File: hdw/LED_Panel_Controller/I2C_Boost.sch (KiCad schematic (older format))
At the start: 7 parts, among them U1301 LTC1694, U1302 AT24CS32-STUM, U1303 MCP9804

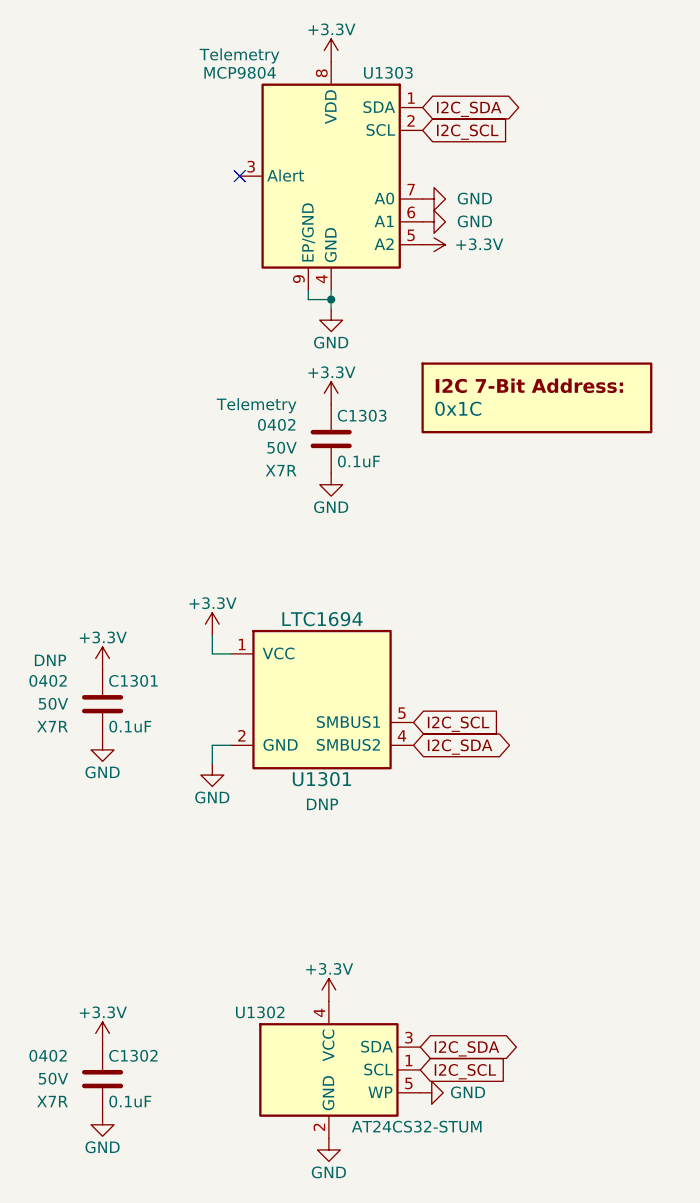
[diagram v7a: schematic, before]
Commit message: separated function groups on PCB
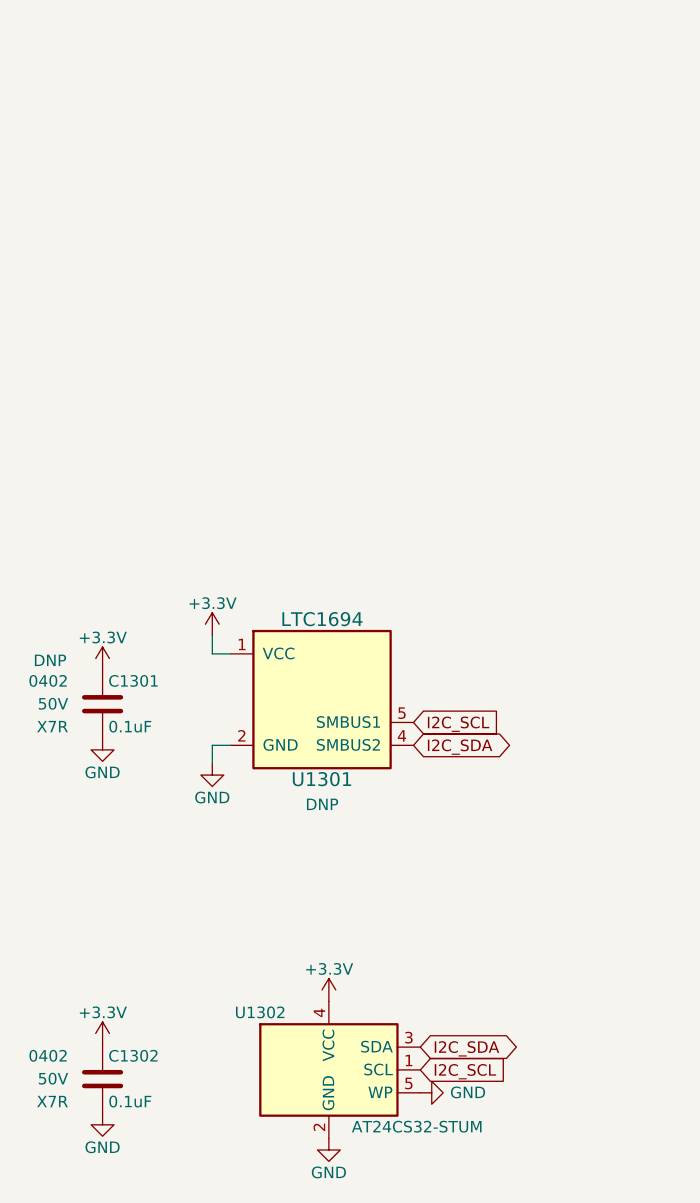
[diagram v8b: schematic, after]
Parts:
- removed C1303: 0.1uF, Capacitors_SMD:C_0402, symbol Custom_Library:C_Custom
- removed DOC1301: 0x1C, symbol Custom_Library:I2C_Address
- removed U1303: MCP9804, Package_DFN_QFN:DFN-8-1EP_3x2mm_P0.5mm_EP1.3x1.5mm, symbol Sensor_Temperature:MCP9804_DFN
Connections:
- no-connect marks 1 -> 0
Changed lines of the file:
@@
 	0    -1   -1   0
 $EndComp
-$Comp
-L power:GND #PWR?
-U 1 1 6061CC13
-P 5340 2050
-AR Path="/5B3E071A/6061CC13" Ref="#PWR?"  Part="1"
-AR Path="/5E0652BA/6061CC13" Ref="#PWR?"  Part="1"
-AR Path="/5E0A0E29/6061CC13" Ref="#PWR?"  Part="1"
-AR Path="/5E052856/6061CC13" Ref="#PWR?"  Part="1"
-AR Path="/5EAE2D84/6061CC13" Ref="#PWR?"  Part="1"
-AR Path="/5F581B58/6061CC13" Ref="#PWR?"  Part="1"
-AR Path="/5F581B77/6061CC13" Ref="#PWR?"  Part="1"
-AR Path="/5F581BB7/6061CC13" Ref="#PWR?"  Part="1"
-AR Path="/5F582A7C/6061CC13" Ref="#PWR01310"  Part="1"
-F 0 "#PWR01310" H 5340 1800 50  0001 C CNN
-F 1 "GND" H 5340 1900 50  0000 C CNN
-F 2 "" H 5340 2050 50  0001 C CNN
-F 3 "" H 5340 2050 50  0001 C CNN
-	1    5340 2050
-	-1   0    0    -1
-$EndComp
-Wire Wire Line
-	5340 2050 5340 2010
-Wire Wire Line
-	5340 2010 5340 1970
-Wire Wire Line
-	5340 2010 5240 2010
-Wire Wire Line
-	5240 2010 5240 1970
-Connection ~ 5340 2010
-$Comp
-L power:+3.3V #PWR?
-U 1 1 6061CC1E
-P 5340 970
-AR Path="/5E0652BA/6061CC1E" Ref="#PWR?"  Part="1"
-AR Path="/5E0A0E29/6061CC1E" Ref="#PWR?"  Part="1"
-AR Path="/5E052856/6061CC1E" Ref="#PWR?"  Part="1"
-AR Path="/5EAE2D84/6061CC1E" Ref="#PWR?"  Part="1"
-AR Path="/5F581B58/6061CC1E" Ref="#PWR?"  Part="1"
-AR Path="/5F581B77/6061CC1E" Ref="#PWR?"  Part="1"
-AR Path="/5F581BB7/6061CC1E" Ref="#PWR?"  Part="1"
-AR Path="/5F582A7C/6061CC1E" Ref="#PWR01309"  Part="1"
-F 0 "#PWR01309" H 5340 820 50  0001 C CNN
-F 1 "+3.3V" H 5340 1110 50  0000 C CNN
-F 2 "" H 5340 970 50  0001 C CNN
-F 3 "" H 5340 970 50  0001 C CNN
-	1    5340 970
-	-1   0    0    -1
-$EndComp
-$Comp
-L Sensor_Temperature:MCP9804_DFN U?
-U 1 1 6061CC26
-P 5340 1470
-AR Path="/5B3E071A/6061CC26" Ref="U?"  Part="1"
-AR Path="/5E0652BA/6061CC26" Ref="U?"  Part="1"
-AR Path="/5E0A0E29/6061CC26" Ref="U?"  Part="1"
-AR Path="/5E052856/6061CC26" Ref="U?"  Part="1"
-AR Path="/5EAE2D84/6061CC26" Ref="U?"  Part="1"
-AR Path="/5F581B58/6061CC26" Ref="U?"  Part="1"
-AR Path="/5F581B77/6061CC26" Ref="U?"  Part="1"
-AR Path="/5F581BB7/6061CC26" Ref="U?"  Part="1"
-AR Path="/5F582A7C/6061CC26" Ref="U1303"  Part="1"
-F 0 "U1303" H 5090 1920 50  0000 C CNN
-F 1 "MCP9804" H 5740 1920 50  0000 C CNN
-F 2 "Package_DFN_QFN:DFN-8-1EP_3x2mm_P0.5mm_EP1.3x1.5mm" H 4240 970 50  0001 C CNN
-F 3 "http://ww1.microchip.com/downloads/en/DeviceDoc/22203b.pdf" H 5090 1920 50  0001 C CNN
-F 4 "MCP9804T-E/MCCT-ND" H 5340 1470 50  0001 C CNN "Digi-Key PN"
-F 5 "Telemetry" H 5740 2000 50  0000 C CNN "Configuration"
-	1    5340 1470
-	-1   0    0    -1
-$EndComp
-Text GLabel 5740 1270 2    50   Input ~ 0
-I2C_SCL
-Text GLabel 5740 1170 2    50   BiDi ~ 0
-I2C_SDA
-NoConn ~ 4940 1470
-$Comp
-L power:+3.3V #PWR?
-U 1 1 6061CC2F
-P 5340 2470
-AR Path="/5E0652BA/6061CC2F" Ref="#PWR?"  Part="1"
-AR Path="/5E0A0E29/6061CC2F" Ref="#PWR?"  Part="1"
-AR Path="/5E052856/6061CC2F" Ref="#PWR?"  Part="1"
-AR Path="/5EAE2D84/6061CC2F" Ref="#PWR?"  Part="1"
-AR Path="/5F581B58/6061CC2F" Ref="#PWR?"  Part="1"
-AR Path="/5F581B77/6061CC2F" Ref="#PWR?"  Part="1"
-AR Path="/5F581BB7/6061CC2F" Ref="#PWR?"  Part="1"
-AR Path="/5F582A7C/6061CC2F" Ref="#PWR01311"  Part="1"
-F 0 "#PWR01311" H 5340 2320 50  0001 C CNN
-F 1 "+3.3V" H 5340 2610 50  0000 C CNN
-F 2 "" H 5340 2470 50  0001 C CNN
-F 3 "" H 5340 2470 50  0001 C CNN
-	1    5340 2470
-	1    0    0    -1
-$EndComp
-$Comp
-L power:GND #PWR?
-U 1 1 6061CC35
-P 5340 2770
-AR Path="/5E0652BA/6061CC35" Ref="#PWR?"  Part="1"
-AR Path="/5E0A0E29/6061CC35" Ref="#PWR?"  Part="1"
-AR Path="/5E052856/6061CC35" Ref="#PWR?"  Part="1"
-AR Path="/5EAE2D84/6061CC35" Ref="#PWR?"  Part="1"
-AR Path="/5F581B58/6061CC35" Ref="#PWR?"  Part="1"
-AR Path="/5F581B77/6061CC35" Ref="#PWR?"  Part="1"
-AR Path="/5F581BB7/6061CC35" Ref="#PWR?"  Part="1"
-AR Path="/5F582A7C/6061CC35" Ref="#PWR01312"  Part="1"
-F 0 "#PWR01312" H 5340 2520 50  0001 C CNN
-F 1 "GND" H 5340 2620 50  0000 C CNN
-F 2 "" H 5340 2770 50  0001 C CNN
-F 3 "" H 5340 2770 50  0001 C CNN
-	1    5340 2770
-	1    0    0    -1
-$EndComp
-$Comp
-L Custom_Library:I2C_Address DOC?
-U 1 1 6061CC3B
-P 6240 2490
-AR Path="/5E0652BA/6061CC3B" Ref="DOC?"  Part="1"
-AR Path="/5E0A0E29/6061CC3B" Ref="DOC?"  Part="1"
-AR Path="/5E052856/6061CC3B" Ref="DOC?"  Part="1"
-AR Path="/5EAE2D84/6061CC3B" Ref="DOC?"  Part="1"
-AR Path="/5F581B58/6061CC3B" Ref="DOC?"  Part="1"
-AR Path="/5F581B77/6061CC3B" Ref="DOC?"  Part="1"
-AR Path="/5F581BB7/6061CC3B" Ref="DOC?"  Part="1"
-AR Path="/5F582A7C/6061CC3B" Ref="DOC1301"  Part="1"
-F 0 "DOC1301" H 6240 2740 60  0001 C CNN
-F 1 "0x1C" H 5790 2490 60  0000 L CNN
-F 2 "" H 6240 2840 60  0001 C CNN
-F 3 "" H 6240 2840 60  0001 C CNN
-	1    6240 2490
-	1    0    0    -1
-$EndComp
-$Comp
-L Custom_Library:C_Custom C?
-U 1 1 6061CC45
-P 5340 2620
-AR Path="/5B3E071A/6061CC45" Ref="C?"  Part="1"
-AR Path="/5E0652BA/6061CC45" Ref="C?"  Part="1"
-AR Path="/5E0A0E29/6061CC45" Ref="C?"  Part="1"
-AR Path="/5E052856/6061CC45" Ref="C?"  Part="1"
-AR Path="/5EAE2D84/6061CC45" Ref="C?"  Part="1"
-AR Path="/5F581B58/6061CC45" Ref="C?"  Part="1"
-AR Path="/5F581B77/6061CC45" Ref="C?"  Part="1"
-AR Path="/5F581BB7/6061CC45" Ref="C?"  Part="1"
-AR Path="/5F582A7C/6061CC45" Ref="C1303"  Part="1"
-F 0 "C1303" H 5365 2720 50  0000 L CNN
-F 1 "0.1uF" H 5365 2520 50  0000 L CNN
-F 2 "Capacitors_SMD:C_0402" H 5378 2470 50  0001 C CNN
-F 3 "" H 5365 2720 50  0001 C CNN
-F 4 "0402" H 5190 2680 50  0000 R CNN "display_footprint"
-F 5 "50V" H 5190 2580 50  0000 R CNN "Voltage"
-F 6 "X7R" H 5190 2480 50  0000 R CNN "Dielectric"
-F 7 "Telemetry" H 5190 2770 50  0000 R CNN "Configuration"
-F 8 "490-10701-1-ND" H 5340 2620 50  0001 C CNN "Digi-Key PN"
-	1    5340 2620
-	1    0    0    -1
-$EndComp
-$Comp
-L power:GND #PWR?
-U 1 1 6076C67B
-P 5740 1570
-AR Path="/5B3E071A/6076C67B" Ref="#PWR?"  Part="1"
-AR Path="/5E0652BA/6076C67B" Ref="#PWR?"  Part="1"
-AR Path="/5E0A0E29/6076C67B" Ref="#PWR?"  Part="1"
-AR Path="/5E052856/6076C67B" Ref="#PWR?"  Part="1"
-AR Path="/5EAE2D84/6076C67B" Ref="#PWR?"  Part="1"
-AR Path="/5F581B58/6076C67B" Ref="#PWR?"  Part="1"
-AR Path="/5F581B77/6076C67B" Ref="#PWR?"  Part="1"
-AR Path="/5F5829EF/6076C67B" Ref="#PWR?"  Part="1"
-AR Path="/5F582A7C/6076C67B" Ref="#PWR01314"  Part="1"
-F 0 "#PWR01314" H 5740 1320 50  0001 C CNN
-F 1 "GND" V 5740 1420 50  0000 R CNN
-F 2 "" H 5740 1570 50  0001 C CNN
-F 3 "" H 5740 1570 50  0001 C CNN
-	1    5740 1570
-	0    -1   1    0
-$EndComp
-$Comp
-L power:+3.3V #PWR?
-U 1 1 6076C681
-P 5740 1770
-AR Path="/5E0652BA/6076C681" Ref="#PWR?"  Part="1"
-AR Path="/5E0A0E29/6076C681" Ref="#PWR?"  Part="1"
-AR Path="/5E052856/6076C681" Ref="#PWR?"  Part="1"
-AR Path="/5EAE2D84/6076C681" Ref="#PWR?"  Part="1"
-AR Path="/5F581B58/6076C681" Ref="#PWR?"  Part="1"
-AR Path="/5F581B77/6076C681" Ref="#PWR?"  Part="1"
-AR Path="/5F5829EF/6076C681" Ref="#PWR?"  Part="1"
-AR Path="/5F582A7C/6076C681" Ref="#PWR01316"  Part="1"
-F 0 "#PWR01316" H 5740 1620 50  0001 C CNN
-F 1 "+3.3V" V 5740 1910 50  0000 L CNN
-F 2 "" H 5740 1770 50  0001 C CNN
-F 3 "" H 5740 1770 50  0001 C CNN
-	1    5740 1770
-	0    1    -1   0
-$EndComp
-$Comp
-L power:GND #PWR?
-U 1 1 6076C8FF
-P 5740 1670
-AR Path="/5B3E071A/6076C8FF" Ref="#PWR?"  Part="1"
-AR Path="/5E0652BA/6076C8FF" Ref="#PWR?"  Part="1"
-AR Path="/5E0A0E29/6076C8FF" Ref="#PWR?"  Part="1"
-AR Path="/5E052856/6076C8FF" Ref="#PWR?"  Part="1"
-AR Path="/5EAE2D84/6076C8FF" Ref="#PWR?"  Part="1"
-AR Path="/5F581B58/6076C8FF" Ref="#PWR?"  Part="1"
-AR Path="/5F581B77/6076C8FF" Ref="#PWR?"  Part="1"
-AR Path="/5F5829EF/6076C8FF" Ref="#PWR?"  Part="1"
-AR Path="/5F582A7C/6076C8FF" Ref="#PWR01315"  Part="1"
-F 0 "#PWR01315" H 5740 1420 50  0001 C CNN
-F 1 "GND" V 5740 1520 50  0000 R CNN
-F 2 "" H 5740 1670 50  0001 C CNN
-F 3 "" H 5740 1670 50  0001 C CNN
-	1    5740 1670
-	0    -1   1    0
-$EndComp
 $EndSCHEMATC
